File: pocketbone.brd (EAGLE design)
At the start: 55 x 35 mm, 61 parts, among them J1 USD_CONNECTOR, U1 24LC_32AT-I/OT, U2 OSD3358, U3 SN74LVC1G07_DCK_5, Y1 CM200C-32.768KAZF-UT, Y2 445C33D24M00000

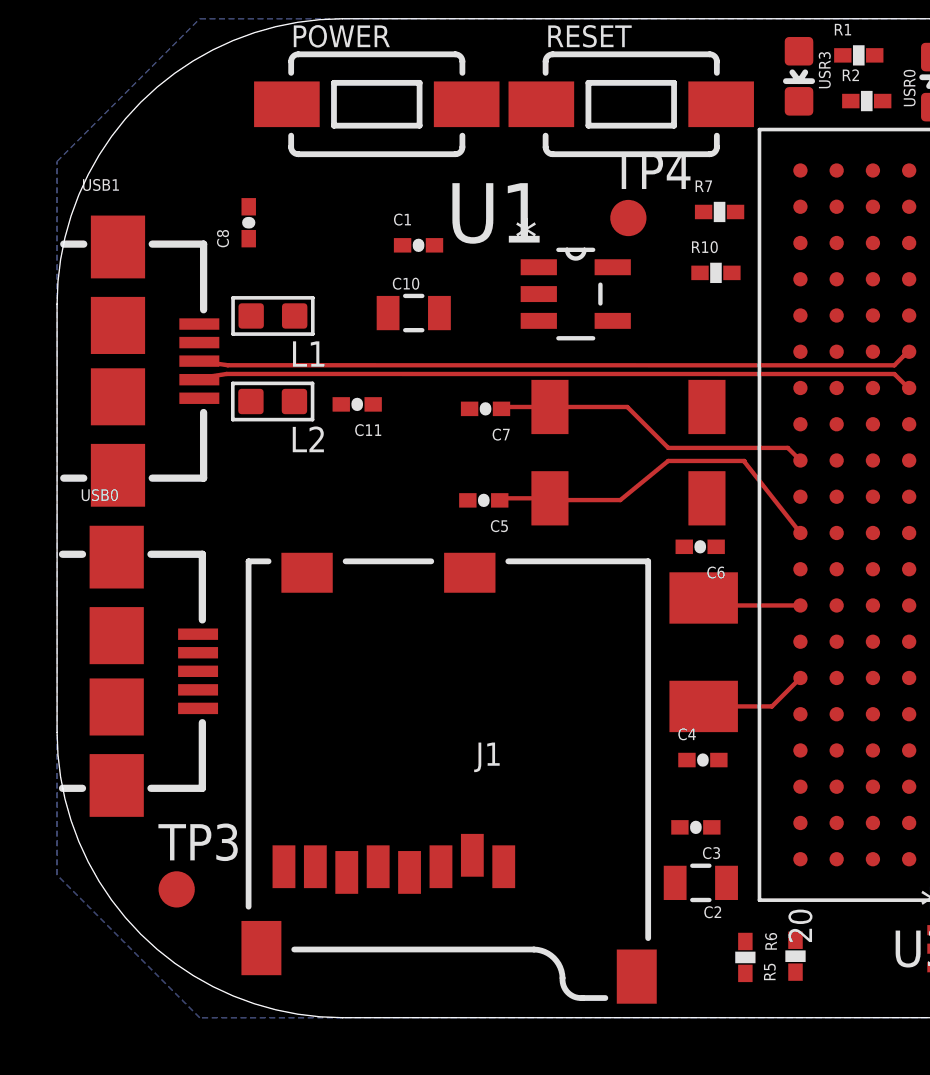
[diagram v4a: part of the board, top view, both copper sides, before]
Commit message: Resize some silkscreen
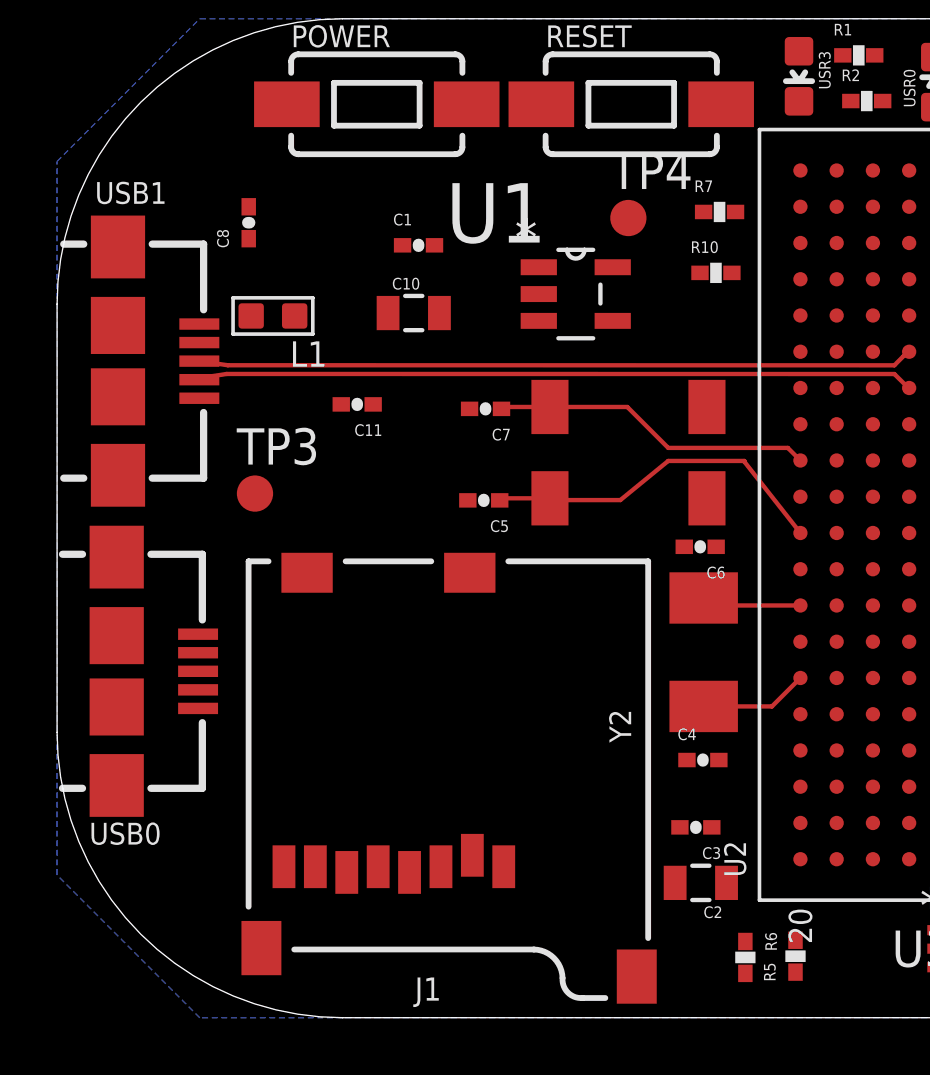
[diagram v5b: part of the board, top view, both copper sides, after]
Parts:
- removed L2: 120, Seeed-OPL-Inductor:L0603
- moved TP3 14.1 mm to (6.93, 18.4)
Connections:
- removed net N$128: L2.2, USB1.GND, USB1.SHIELD1, USB1.SHIELD2, USB1.SHIELD3, USB1.SHIELD4
- net GND: now also USB1.GND, USB1.SHIELD1, USB1.SHIELD2, USB1.SHIELD3, USB1.SHIELD4; no longer L2.1
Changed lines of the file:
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@@
 <element name="USR3" library="BeagleBone_Blue" package="LED-0603" value="BLUE" x="25.9948" y="32.9842" rot="R180"/>
 <element name="PWR" library="BeagleBone_Blue" package="LED-0603" value="BLUE" x="39.6434" y="32.8744" rot="R180"/>
-<element name="J1" library="pocketbone" package="MICRO-SD-SOCKET-PP" value="USD_CONNECTOR" x="6.7098" y="15.9898" rot="R180">
+<element name="J1" library="pocketbone" package="MICRO-SD-SOCKET-PP" value="USD_CONNECTOR" x="6.7098" y="15.9898" smashed="yes" rot="R180">
 <attribute name="PROD_ID" value="CONN-07820" x="6.7098" y="15.9898" size="1.778" layer="27" rot="R180" display="off"/>
-</element>
-<element name="L2" library="Seeed-OPL-Inductor" package="L0603" value="120" x="7.554" y="21.5896" rot="R180"/>
+<attribute name="NAME" x="13.4662" y="1.4102" size="0.8128" layer="25" rot="R180"/>
+<attribute name="VALUE" x="18.343" y="10.4526" size="0.8128" layer="27" rot="R180"/>
+</element>
 <element name="L1" library="Seeed-OPL-Inductor" package="L0603" value="120" x="7.5626" y="24.5864" rot="R180"/>
 <element name="R27" library="Strawson_Eagle_Lib" package="0402-RES" value="100K,1%" x="48.8912" y="32.192659375"/>
@@
 <attribute name="DESCRIPTION" value="Single Buffer/Driver With Open-Drain Output" x="32.1146" y="2.4178" size="1.778" layer="27" display="off"/>
 </element>
-<element name="USB0" library="pocketbone" package="USB-AB-MICRO-SMD" value="USB-MICRO-SMD" x="2.09" y="12.1372"/>
-<element name="USB1" library="pocketbone" package="USB-AB-MICRO-SMD" value="USB-MICRO-SMD" x="2.134" y="23.0042"/>
+<element name="USB0" library="pocketbone" package="USB-AB-MICRO-SMD" value="USB-MICRO-SMD" x="2.09" y="12.1372" smashed="yes">
+<attribute name="NAME" x="1.1248" y="6.0666" size="0.762" layer="25"/>
+<attribute name="VALUE" x="2.2138" y="10.1164" size="0.4064" layer="27" rot="R90"/>
+</element>
+<element name="USB1" library="pocketbone" package="USB-AB-MICRO-SMD" value="USB-MICRO-SMD" x="2.134" y="23.0042" smashed="yes">
+<attribute name="NAME" x="1.3212" y="28.516" size="0.762" layer="25"/>
+<attribute name="VALUE" x="2.3196" y="20.8284" size="0.4064" layer="27" rot="R90"/>
+</element>
 <element name="Y1" library="pocketbone" package="CM200C-32.768KAZF-UT" value="CM200C-32.768KAZF-UT" x="15.999" y="15.658"/>
 <element name="Y2" library="pocketbone" package="445C33D24M00000" value="445C33D24M00000" x="25.1948" y="9.636" rot="R90"/>
-<element name="TP3" library="testpad" package="B1,27" value="TPSQB1,27" x="4.191" y="4.4958">
-<attribute name="TP_SIGNAL_NAME" value="GND" x="4.191" y="4.4958" size="1.778" layer="27" display="off"/>
+<element name="TP3" library="testpad" package="B1,27" value="TPSQB1,27" x="6.9342" y="18.3642">
+<attribute name="TP_SIGNAL_NAME" value="GND" x="6.9342" y="18.3642" size="1.778" layer="27" display="off"/>
 </element>
 <element name="POWER" library="SparkFun-Electromechanical" package="TACTILE-SWITCH-1101NE" value="SWITCH-MOMENTARY-2SMD-1101NE" x="11.2014" y="32.004">
@@
 <contactref element="R28" pad="1"/>
 <contactref element="R23" pad="1"/>
-<contactref element="L2" pad="1"/>
 <contactref element="C11" pad="2"/>
 <contactref element="C10" pad="2"/>
@@
 <vertex x="50" y="0"/>
 </polygon>
+<contactref element="USB1" pad="GND"/>
+<contactref element="USB1" pad="SHIELD3"/>
+<contactref element="USB1" pad="SHIELD4"/>
+<contactref element="USB1" pad="SHIELD1"/>
+<contactref element="USB1" pad="SHIELD2"/>
 <wire x1="48.3324" y1="32.192659375" x2="48.5864" y2="33.564259375" width="0" layer="19" extent="1-1"/>
 <wire x1="46.1734" y1="33.945259375" x2="48.5864" y2="33.564259375" width="0" layer="19" extent="1-1"/>
@@
 <wire x1="35.353" y1="0.798259375" x2="37.5628" y2="3.008059375" width="0" layer="19" extent="1-1"/>
 <wire x1="31.0732" y1="1.7678125" x2="35.353" y2="0.798259375" width="0" layer="19" extent="1-1"/>
+<wire x1="23.4552" y1="4.7244" x2="31.0732" y2="1.7678125" width="0" layer="19" extent="1-1"/>
+<wire x1="22.94" y1="6.669340625" x2="23.4552" y2="4.7244" width="0" layer="19" extent="1-1"/>
+<wire x1="20.3098" y1="1.4398" x2="23.4552" y2="4.7244" width="0" layer="19" extent="1-1"/>
 <wire x1="43.8244" y1="15.7132" x2="52.752" y2="15.301659375" width="0" layer="19" extent="1-1"/>
 <wire x1="42.5544" y1="20.7932" x2="43.8244" y2="15.7132" width="0" layer="19" extent="1-1"/>
@@
 <wire x1="13.2232" y1="27.0616" x2="13.3968" y2="24.6888" width="0" layer="19" extent="1-1"/>
 <wire x1="9.9568" y1="21.4884" x2="13.3968" y2="24.6888" width="0" layer="19" extent="1-1"/>
-<wire x1="8.316" y1="21.5896" x2="9.9568" y2="21.4884" width="0" layer="19" extent="1-1"/>
-<wire x1="16.9668" y1="32.004" x2="13.2232" y2="27.0616" width="0" layer="19" extent="1-1"/>
-<wire x1="6.7148" y1="28.4124" x2="13.2232" y2="27.0616" width="0" layer="19" extent="1-1"/>
-<wire x1="8.0514" y1="32.004" x2="6.7148" y2="28.4124" width="0" layer="19" extent="1-1"/>
-<wire x1="2.09" y1="16.1372" x2="8.316" y2="21.5896" width="0" layer="19" extent="1-1"/>
+<wire x1="6.9342" y1="18.3642" x2="9.9568" y2="21.4884" width="0" layer="19" extent="1-1"/>
+<wire x1="4.984" y1="21.7042" x2="6.9342" y2="18.3642" width="0" layer="19" extent="1-1"/>
+<wire x1="2.134" y1="21.7542" x2="4.984" y2="21.7042" width="0" layer="19" extent="1-1"/>
+<wire x1="2.134" y1="24.2542" x2="2.134" y2="21.7542" width="0" layer="19" extent="1-1"/>
+<wire x1="2.134" y1="27.0042" x2="2.134" y2="24.2542" width="0" layer="19" extent="1-1"/>
+<wire x1="2.134" y1="19.0042" x2="2.134" y2="21.7542" width="0" layer="19" extent="1-1"/>
+<wire x1="2.09" y1="16.1372" x2="2.134" y2="19.0042" width="0" layer="19" extent="1-1"/>
 <wire x1="2.09" y1="13.3872" x2="2.09" y2="16.1372" width="0" layer="19" extent="1-1"/>
 <wire x1="2.09" y1="10.8872" x2="2.09" y2="13.3872" width="0" layer="19" extent="1-1"/>
 <wire x1="2.09" y1="8.1372" x2="2.09" y2="10.8872" width="0" layer="19" extent="1-1"/>
 <wire x1="4.94" y1="10.8372" x2="2.09" y2="10.8872" width="0" layer="19" extent="1-1"/>
-<wire x1="4.191" y1="4.4958" x2="2.09" y2="8.1372" width="0" layer="19" extent="1-1"/>
-<wire x1="7.1598" y1="2.4398" x2="4.191" y2="4.4958" width="0" layer="19" extent="1-1"/>
+<wire x1="6.7148" y1="28.4124" x2="2.134" y2="27.0042" width="0" layer="19" extent="1-1"/>
+<wire x1="8.0514" y1="32.004" x2="6.7148" y2="28.4124" width="0" layer="19" extent="1-1"/>
+<wire x1="16.9668" y1="32.004" x2="13.2232" y2="27.0616" width="0" layer="19" extent="1-1"/>
+<wire x1="7.1598" y1="2.4398" x2="2.09" y2="8.1372" width="0" layer="19" extent="1-1"/>
 <wire x1="10.1498" y1="5.0898" x2="7.1598" y2="2.4398" width="0" layer="19" extent="1-1"/>
-<wire x1="20.3098" y1="1.4398" x2="10.1498" y2="5.0898" width="0" layer="19" extent="1-1"/>
-<wire x1="23.4552" y1="4.7244" x2="20.3098" y2="1.4398" width="0" layer="19" extent="1-1"/>
-<wire x1="22.94" y1="6.669340625" x2="23.4552" y2="4.7244" width="0" layer="19" extent="1-1"/>
 </signal>
 <signal name="VDD_1V8">
@@
 <contactref element="U3" pad="2"/>
 <wire x1="31.0732" y1="2.4178" x2="32.3944" y2="6.8232" width="0" layer="19" extent="1-1"/>
-<wire x1="26.0444" y1="5.5532" x2="32.3944" y2="6.8232" width="0" layer="19" extent="1-1"/>
+<wire x1="26.0444" y1="5.5532" x2="31.0732" y2="2.4178" width="0" layer="19" extent="1-1"/>
 </signal>
 <signal name="PMIC_NWAKEUP">
@@
 <wire x1="22.526" y1="26.096659375" x2="23.2668" y2="32.004" width="0" layer="19" extent="1-1"/>
 <wire x1="38.7444" y1="5.5532" x2="22.526" y2="26.096659375" width="0" layer="19" extent="1-1"/>
-<wire x1="33.156" y1="1.7678125" x2="38.7444" y2="5.5532" width="0" layer="19" extent="1-1"/>
-<wire x1="34.2354" y1="0.798259375" x2="33.156" y2="1.7678125" width="0" layer="19" extent="1-1"/>
+<wire x1="34.2354" y1="0.798259375" x2="38.7444" y2="5.5532" width="0" layer="19" extent="1-1"/>
+<wire x1="33.156" y1="1.7678125" x2="34.2354" y2="0.798259375" width="0" layer="19" extent="1-1"/>
 </signal>
 <signal name="VDD_RTC">
@@
 <contactref element="J1" pad="VCC"/>
 <wire x1="21.6552" y1="4.7244" x2="21.8224" y2="6.669340625" width="0" layer="19" extent="1-1"/>
-<wire x1="12.3498" y1="5.0898" x2="21.8224" y2="6.669340625" width="0" layer="19" extent="1-1"/>
+<wire x1="12.3498" y1="5.0898" x2="21.6552" y2="4.7244" width="0" layer="19" extent="1-1"/>
 </signal>
 <signal name="NTE">
@@
 <wire x1="4.984" y1="23.6542" x2="28.5844" y2="23.3332" width="0" layer="19" extent="1-1"/>
 </signal>
-<signal name="N$128" class="3">
-<contactref element="L2" pad="2"/>
-<contactref element="USB1" pad="SHIELD1"/>
-<contactref element="USB1" pad="SHIELD2"/>
-<contactref element="USB1" pad="SHIELD3"/>
-<contactref element="USB1" pad="SHIELD4"/>
-<contactref element="USB1" pad="GND"/>
-<wire x1="4.984" y1="21.7042" x2="6.792" y2="21.5896" width="0" layer="19" extent="1-1"/>
-<wire x1="2.134" y1="21.7542" x2="4.984" y2="21.7042" width="0" layer="19" extent="1-1"/>
-<wire x1="2.134" y1="24.2542" x2="2.134" y2="21.7542" width="0" layer="19" extent="1-1"/>
-<wire x1="2.134" y1="27.0042" x2="2.134" y2="24.2542" width="0" layer="19" extent="1-1"/>
-<wire x1="2.134" y1="19.0042" x2="2.134" y2="21.7542" width="0" layer="19" extent="1-1"/>
-</signal>
 <signal name="N$129">

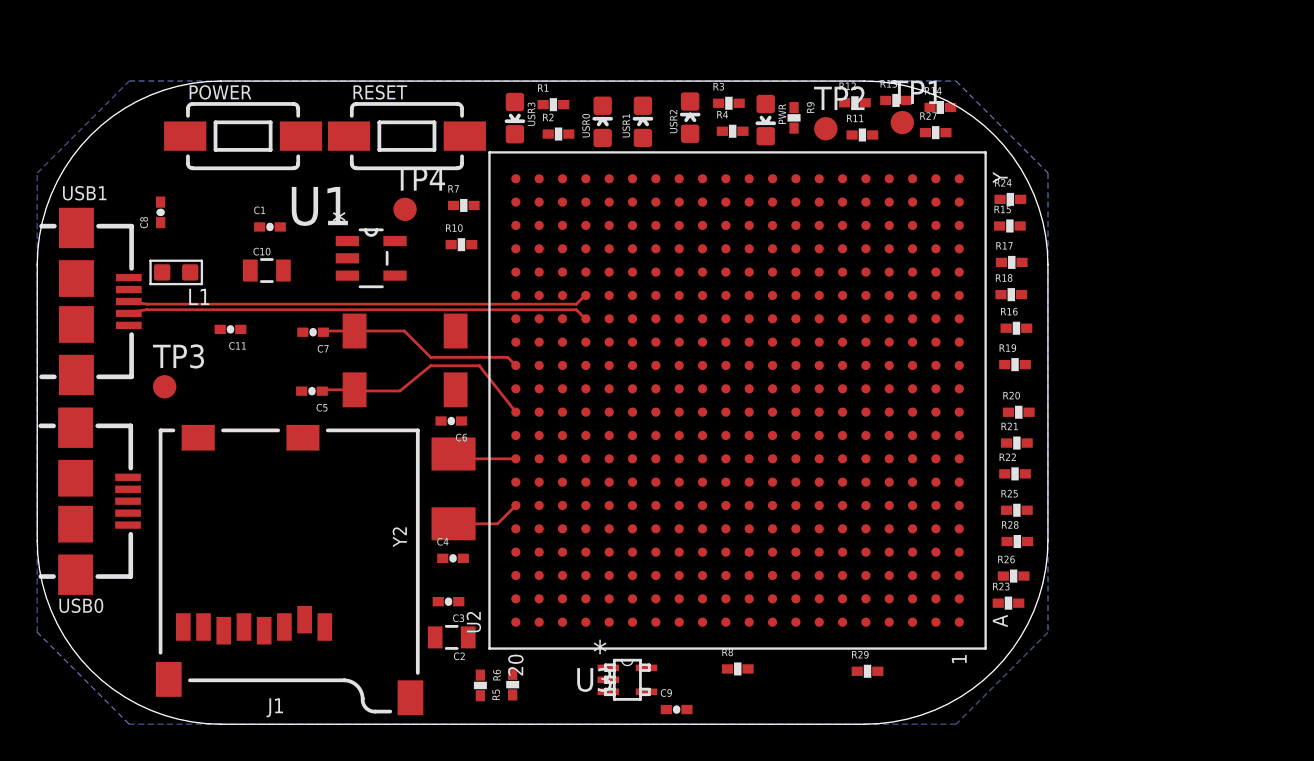
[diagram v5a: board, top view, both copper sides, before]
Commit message: Reposition components
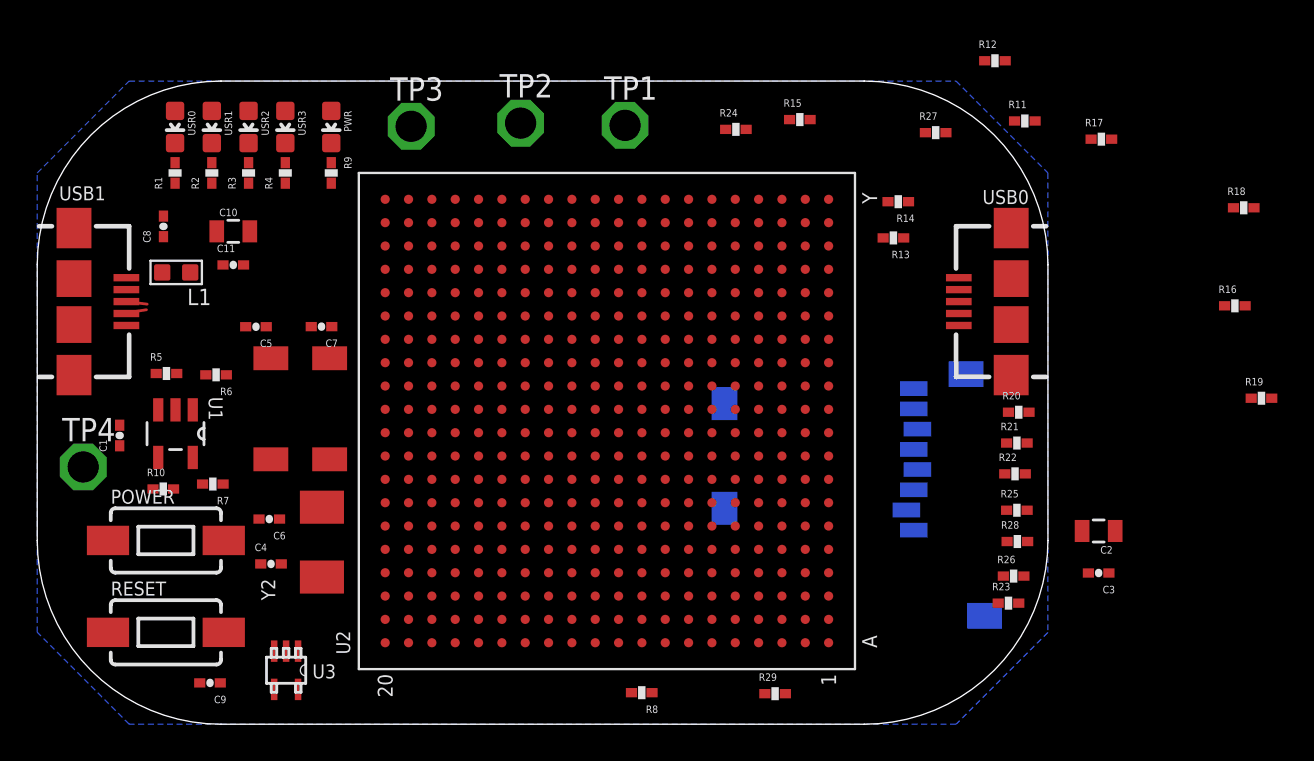
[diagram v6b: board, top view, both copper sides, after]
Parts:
- TP1, TP2, TP3, TP4: value TPSQB1,27 -> TPSQPAD1-17; device testpad:B1,27 -> pocketbone:P1-17
- moved USB0 52.1 mm to (53.0, 23.0), turned to 180 degrees
- moved C2 35.7 mm to (57.8, 10.5)
- moved C3 35.4 mm to (57.8, 8.23)
- moved J1 30.5 mm to (37.0, 19.5), flipped to the bottom, turned to 90 degrees
- moved RESET 30.0 mm to (7.00, 5.00)
- moved R3 26.4 mm to (11.5, 30.0), turned to 90 degrees
- moved C9 25.4 mm to (9.40, 2.25), turned to 180 degrees
- moved R9 25.4 mm to (16.0, 30.0)
- moved R5 25.3 mm to (7.03, 19.1), turned to 0 degrees
- moved R4 24.4 mm to (13.5, 30.0), turned to 90 degrees
- moved USR2 24.0 mm to (11.5, 32.5), turned to 180 degrees
- moved PWR 23.6 mm to (16.0, 32.5)
- moved USR1 23.5 mm to (9.50, 32.5), turned to 180 degrees
- moved USR0 23.3 mm to (7.50, 32.5), turned to 180 degrees
- moved TP4 22.4 mm to (2.50, 14.0)
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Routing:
- net USB1_ID: track 25.2 -> 1.12 mm
- net USB1_DP: track 25.1 -> 1.14 mm
- net N$27: track 12.3 -> 0.00 mm
- net N$26: track 11.3 -> 0.00 mm
- net N$33: track 3.80 -> 0.00 mm
- net N$32: track 3.50 -> 0.00 mm

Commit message: Reposition components
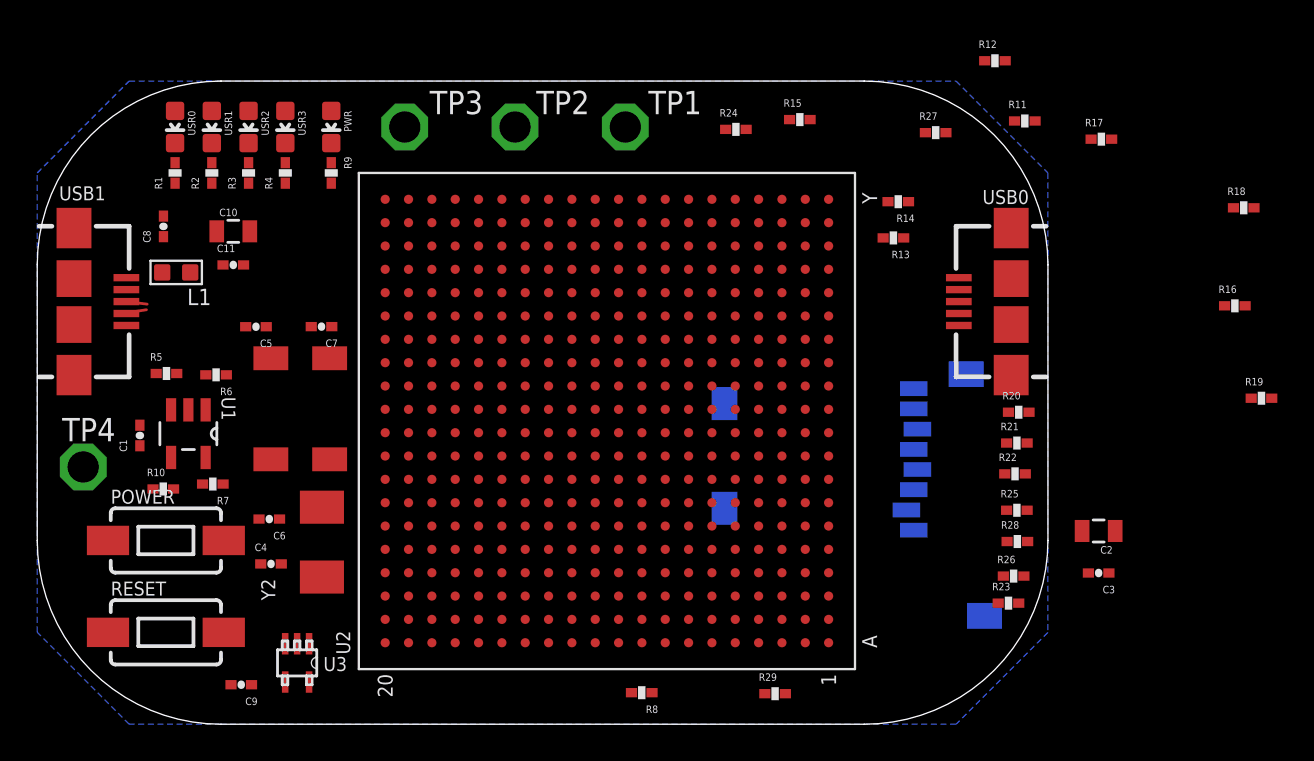
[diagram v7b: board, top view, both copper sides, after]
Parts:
- moved C9 1.70 mm to (11.1, 2.15)
- moved C1 1.10 mm to (5.59, 15.7)
- moved U3 0.72 mm to (14.1, 3.34)
- moved U1 0.70 mm to (8.22, 15.8)
- moved TP2 0.37 mm to (26.0, 32.5)
- moved TP3 0.35 mm to (20.0, 32.5)
- moved TP1 0.09 mm to (32.0, 32.5)
